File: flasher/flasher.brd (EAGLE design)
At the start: 47.4 x 51 mm, 38 parts, among them IC1 ULN2004A_BIG_SMD, Q1 IRF4905, Q2 IRF4905

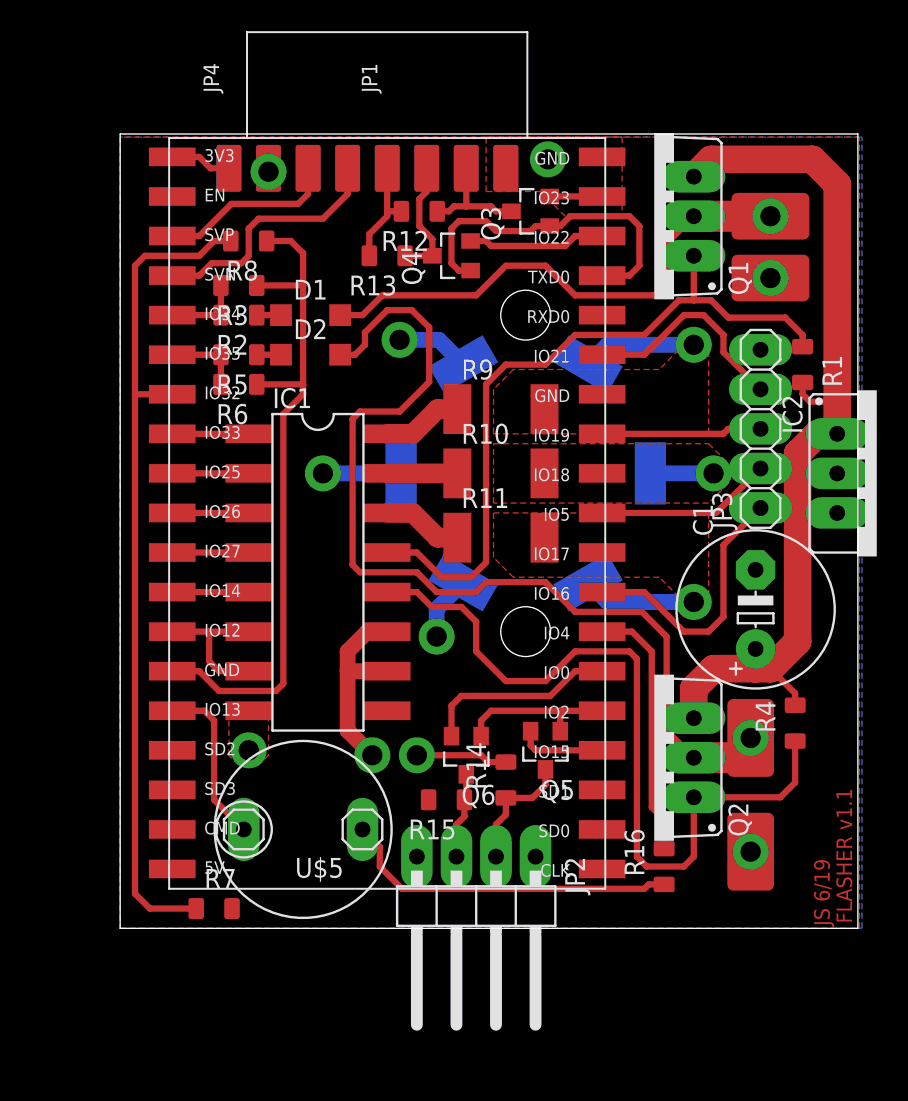
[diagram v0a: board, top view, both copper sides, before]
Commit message: Remove old box outline
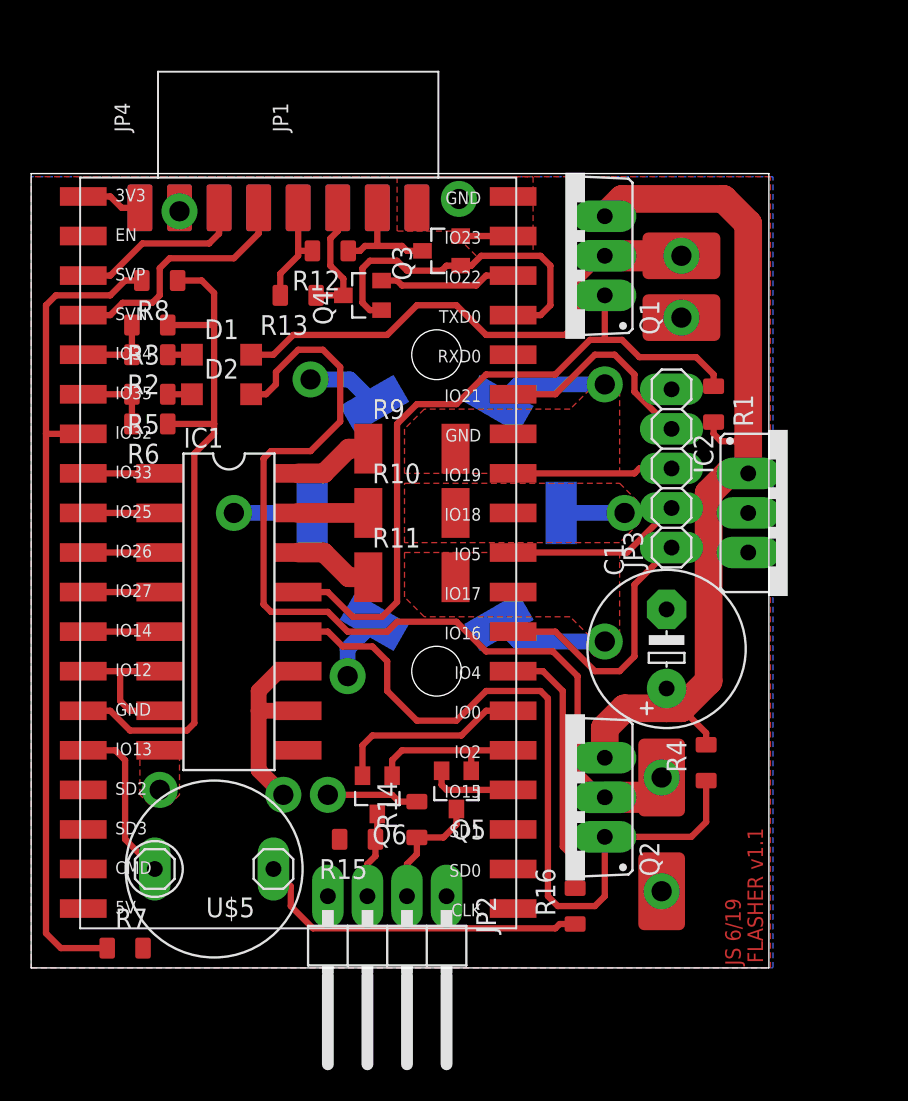
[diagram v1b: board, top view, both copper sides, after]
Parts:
- moved JP1 6.25 mm to (21.0, 50.8)
- moved JP4 6.25 mm to (10.8, 50.8)
- moved Q2 6.25 mm to (34.3, 11.0)
- moved Q5 6.25 mm to (27.3, 11.4)
- moved R16 6.25 mm to (34.9, 3.97)
- moved R4 6.25 mm to (43.3, 13.2)
- moved R6 6.25 mm to (7.62, 34.9)
- moved C1 6.25 mm to (40.8, 20.5)
- moved Q1 6.25 mm to (34.3, 45.7)
- moved Q3 6.25 mm to (26.4, 46.0)
- moved R1 6.25 mm to (43.8, 36.2)
- moved R15 6.25 mm to (21.0, 8.26)
- moved U$1 6.25 mm to (41.8, 45.7)
- moved U$2 6.25 mm to (41.8, 41.8)
- moved R2 6.25 mm to (7.62, 39.4)
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
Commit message: Change resistors value
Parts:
- R1, R4: value 100k -> 33k
- R12, R13, R14, R15: value 18k -> 4k7
- R16: value 18k -> 0R
- R2, R5: value 18k -> 5k6
- R3, R6: value 33k -> 3k3
